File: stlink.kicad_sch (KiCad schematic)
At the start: 36 parts, among them J401 USB_B_Mini, J402 Conn_01x06_Pin, Q401 MMBTA44, U401 STM32F103CBTx, U402 LD1117S33TR_SOT223, U404 ECMF02-2AMX6, Y401 8MHz

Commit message: starting layout
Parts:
- removed Y401: 8MHz, Crystal:Crystal_SMD_HC49-SD_HandSoldering, symbol Device:Crystal
- added Y601: Crystal_GND24, Crystal:Crystal_SMD_EuroQuartz_MQ-4Pin_7.0x5.0mm_HandSoldering, symbol Device:Crystal_GND24
- C603: renamed from C209; footprint Capacitor_SMD:C_0805_2012Metric_Pad1.18x1.45mm_HandSolder -> Capacitor_SMD:C_0603_1608Metric_Pad1.08x0.95mm_HandSolder; Size 0805 -> 0603
- C604: renamed from C210; footprint Capacitor_SMD:C_0805_2012Metric_Pad1.18x1.45mm_HandSolder -> Capacitor_SMD:C_0603_1608Metric_Pad1.08x0.95mm_HandSolder; Size 0805 -> 0603
- C606: renamed from C211; footprint Capacitor_SMD:C_0805_2012Metric_Pad1.18x1.45mm_HandSolder -> Capacitor_SMD:C_0603_1608Metric_Pad1.08x0.95mm_HandSolder; Size 0805 -> 0603
- C607: renamed from C212; footprint Capacitor_SMD:C_0805_2012Metric_Pad1.18x1.45mm_HandSolder -> Capacitor_SMD:C_0603_1608Metric_Pad1.08x0.95mm_HandSolder; Size 0805 -> 0603
- R601: renamed from R219; footprint Resistor_SMD:R_0805_2012Metric_Pad1.20x1.40mm_HandSolder -> Resistor_SMD:R_0603_1608Metric_Pad0.98x0.95mm_HandSolder
- R602: renamed from R220; footprint Resistor_SMD:R_0805_2012Metric_Pad1.20x1.40mm_HandSolder -> Resistor_SMD:R_0603_1608Metric_Pad0.98x0.95mm_HandSolder
- R603: renamed from R221; footprint Resistor_SMD:R_0805_2012Metric_Pad1.20x1.40mm_HandSolder -> Resistor_SMD:R_0603_1608Metric_Pad0.98x0.95mm_HandSolder
- R604: renamed from R222; footprint Resistor_SMD:R_0805_2012Metric_Pad1.20x1.40mm_HandSolder -> Resistor_SMD:R_0603_1608Metric_Pad0.98x0.95mm_HandSolder
- R605: renamed from R223; footprint Resistor_SMD:R_0805_2012Metric_Pad1.20x1.40mm_HandSolder -> Resistor_SMD:R_0603_1608Metric_Pad0.98x0.95mm_HandSolder
- R606: renamed from R224; footprint Resistor_SMD:R_0805_2012Metric_Pad1.20x1.40mm_HandSolder -> Resistor_SMD:R_0603_1608Metric_Pad0.98x0.95mm_HandSolder
- R607: renamed from R217; footprint Resistor_SMD:R_0805_2012Metric_Pad1.20x1.40mm_HandSolder -> Resistor_SMD:R_0603_1608Metric_Pad0.98x0.95mm_HandSolder
- R608: renamed from R218; footprint Resistor_SMD:R_0805_2012Metric_Pad1.20x1.40mm_HandSolder -> Resistor_SMD:R_0603_1608Metric_Pad0.98x0.95mm_HandSolder
- R609: renamed from R225; footprint Resistor_SMD:R_0805_2012Metric_Pad1.20x1.40mm_HandSolder -> Resistor_SMD:R_0603_1608Metric_Pad0.98x0.95mm_HandSolder
- R610: renamed from R229; footprint Resistor_SMD:R_0805_2012Metric_Pad1.20x1.40mm_HandSolder -> Resistor_SMD:R_0603_1608Metric_Pad0.98x0.95mm_HandSolder
- R611: renamed from R213; footprint Resistor_SMD:R_0805_2012Metric_Pad1.20x1.40mm_HandSolder -> Resistor_SMD:R_0603_1608Metric_Pad0.98x0.95mm_HandSolder
- R612: renamed from R212; footprint Resistor_SMD:R_0805_2012Metric_Pad1.20x1.40mm_HandSolder -> Resistor_SMD:R_0603_1608Metric_Pad0.98x0.95mm_HandSolder
- R613: renamed from R216; footprint Resistor_SMD:R_0805_2012Metric_Pad1.20x1.40mm_HandSolder -> Resistor_SMD:R_0603_1608Metric_Pad0.98x0.95mm_HandSolder
- R614: renamed from R215; footprint Resistor_SMD:R_0805_2012Metric_Pad1.20x1.40mm_HandSolder -> Resistor_SMD:R_0603_1608Metric_Pad0.98x0.95mm_HandSolder
- R615: renamed from R230; footprint Resistor_SMD:R_0805_2012Metric_Pad1.20x1.40mm_HandSolder -> Resistor_SMD:R_0603_1608Metric_Pad0.98x0.95mm_HandSolder
- R616: renamed from R231; footprint Resistor_SMD:R_0805_2012Metric_Pad1.20x1.40mm_HandSolder -> Resistor_SMD:R_0603_1608Metric_Pad0.98x0.95mm_HandSolder
- renumbered C217 to C601, C216 to C602, C215 to C605, C214 to C608, C213 to C609, D402 to D601, D401 to D602, D403 to D603, D404 to D604, J402 to J601, J401 to J602, Q401 to Q601, U404 to U601, U402 to U602, U401 to U603
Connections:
- net GND: now also Y601.2, Y601.4
- net OSC_IN: now also Y601.3
- net OSC_OUT: now also Y601.1
- net at R602.2: now also U601.5 (D-_out); no longer U601.2 (D-_in)
- net at U603.32 (PA11): now also U601.2 (D-_in); no longer U601.5 (D-_out)
- net at U603.33 (PA12): now also U601.1 (D+_in); no longer U601.6 (D+_out)
- net at R601.2: now also U601.6 (D+_out); no longer U601.1 (D+_in)

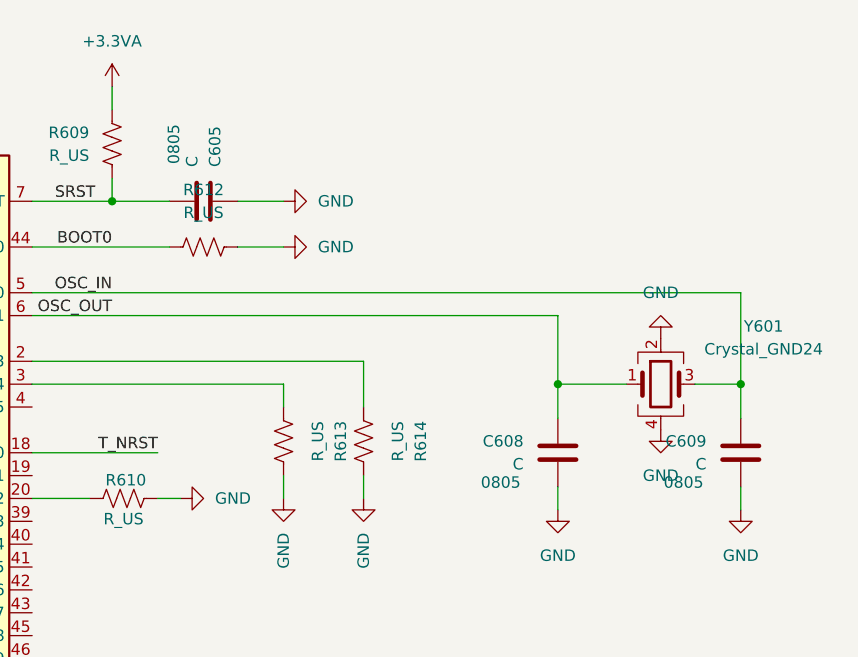
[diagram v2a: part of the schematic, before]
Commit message: Add net class
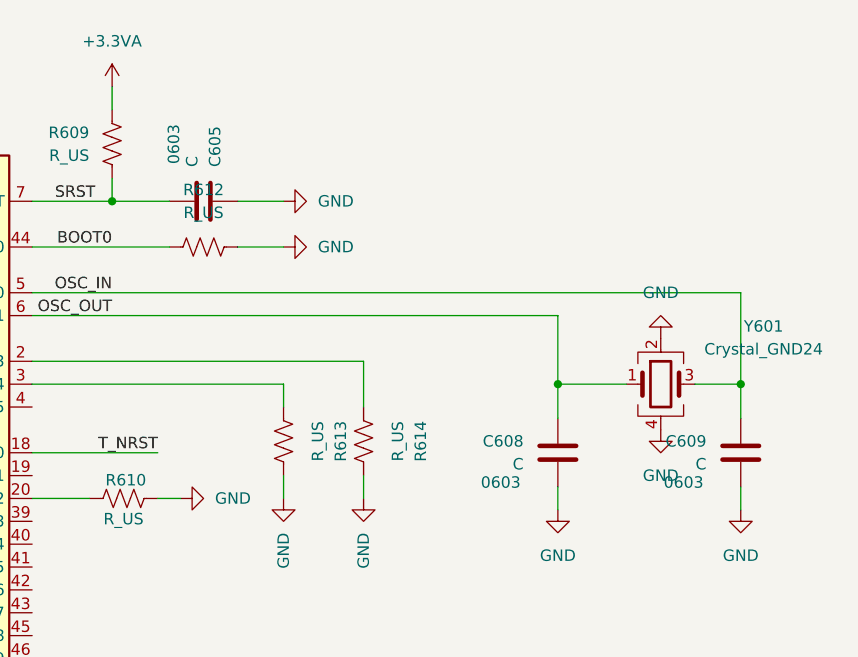
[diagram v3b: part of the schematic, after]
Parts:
- C605, C608, C609: footprint Capacitor_SMD:C_0805_2012Metric_Pad1.18x1.45mm_HandSolder -> Capacitor_SMD:C_0603_1608Metric_Pad1.08x0.95mm_HandSolder; Size 0805 -> 0603
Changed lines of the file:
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@@
 			)
 		)
-		(property "Footprint" "Capacitor_SMD:C_0805_2012Metric_Pad1.18x1.45mm_HandSolder"
+		(property "Footprint" "Capacitor_SMD:C_0603_1608Metric_Pad1.08x0.95mm_HandSolder"
 			(at 265.7348 72.39 0)
 			(effects
@@
 			)
 		)
-		(property "Size" "0805"
+		(property "Size" "0603"
 			(at 260.35 71.882 0)
 			(effects
@@
 			)
 		)
-		(property "Footprint" "Capacitor_SMD:C_0805_2012Metric_Pad1.18x1.45mm_HandSolder"
+		(property "Footprint" "Capacitor_SMD:C_0603_1608Metric_Pad1.08x0.95mm_HandSolder"
 			(at 245.4148 72.39 0)
 			(effects
@@
 			)
 		)
-		(property "Size" "0805"
+		(property "Size" "0603"
 			(at 240.03 71.882 0)
 			(effects
@@
 			)
 		)
-		(property "Footprint" "Capacitor_SMD:C_0805_2012Metric_Pad1.18x1.45mm_HandSolder"
+		(property "Footprint" "Capacitor_SMD:C_0603_1608Metric_Pad1.08x0.95mm_HandSolder"
 			(at 203.2 39.6748 0)
 			(effects
@@
 			)
 		)
-		(property "Size" "0805"
+		(property "Size" "0603"
 			(at 203.708 34.29 0)
 			(effects
